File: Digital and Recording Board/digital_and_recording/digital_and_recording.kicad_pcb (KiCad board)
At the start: 4 copper layers, 47 x 106.3 mm, 40 parts, among them J1 Headphones, J2 Screen, J3 USB_Breakout, J4 Joystick, J6 MINIFIT-2-VERT, J7 MINIFIT-2-VERT, J8 MINIFIT-2-VERT, U1 Daisy_Seed, U2 Daisy_Seed_Recording, U3 Bypass 2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

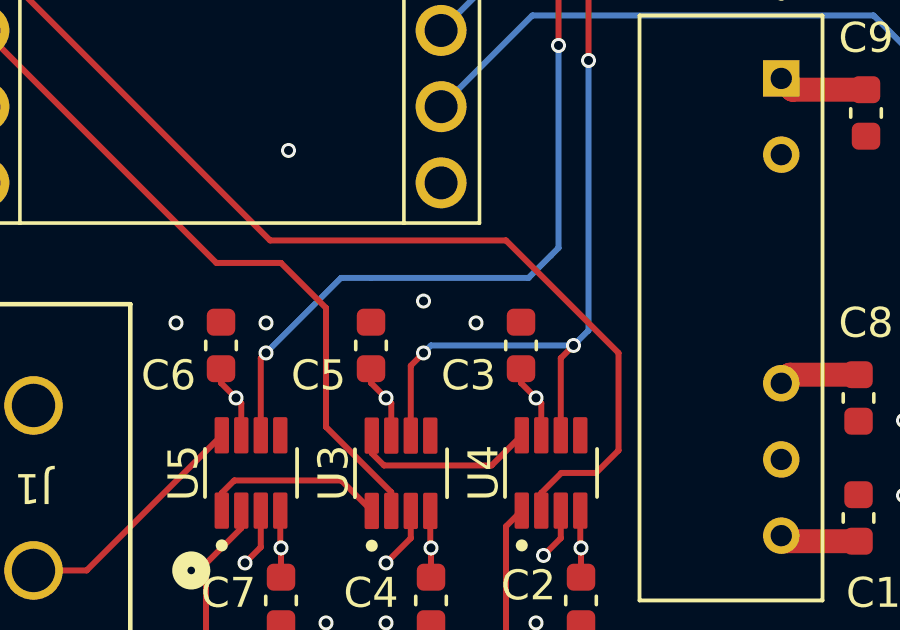
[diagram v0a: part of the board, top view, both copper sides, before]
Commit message: Reduced minimum clearance on digicorder
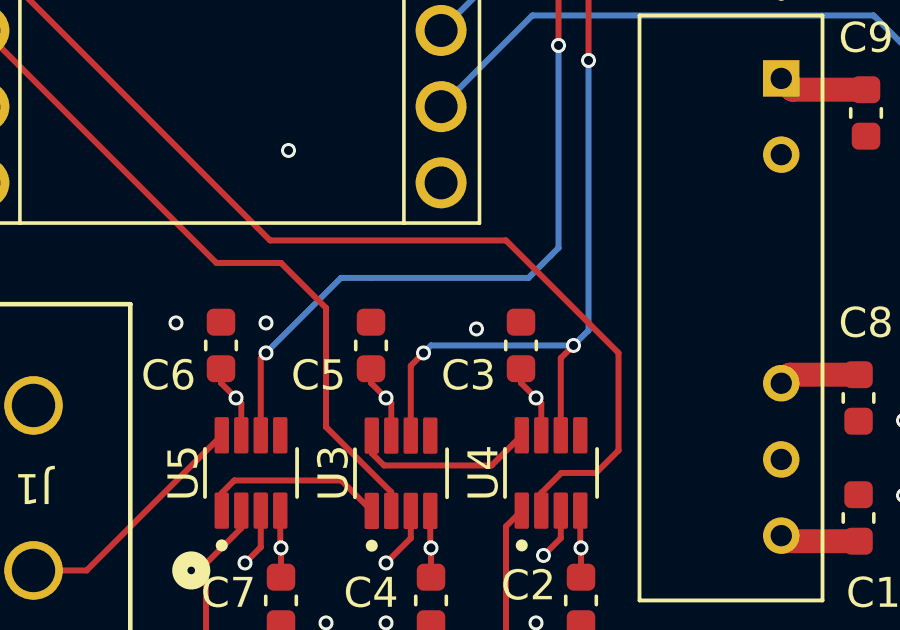
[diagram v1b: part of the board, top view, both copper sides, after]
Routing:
- net GND: vias 51 -> 50
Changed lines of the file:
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@@
 	)
 	(via
-		(at 147 128.75)
+		(at 147.0152 128.95)
 		(size 0.5)
 		(drill 0.3)
@@
 	(via
 		(at 134.25 117.25)
-		(size 0.5)
-		(drill 0.3)
-		(layers "F.Cu" "B.Cu")
-		(free yes)
-		(net 1)
-	)
-	(via
-		(at 145.25 128.02)
 		(size 0.5)
 		(drill 0.3)
@@
 		(priority 5)
 		(connect_pads
-			(clearance 0.5)
+			(clearance 0.25)
 		)
 		(min_thickness 0.25)
@@
 		(priority 3)
 		(connect_pads
-			(clearance 0.5)
+			(clearance 0.25)
 		)
 		(min_thickness 0.25)
@@
 		(polygon
 			(pts
-				(xy 157.7 154.4) (xy 157.7 139.8) (xy 158.5 139) (xy 158.5 139) (xy 160.25 137.249999) (xy 160.25 129.5)
-				(xy 159.25 128.5) (xy 127.5 128.5) (xy 127.5 48.25) (xy 134.23 48.25) (xy 134.23 76.309999) (xy 144.726 88.555333)
+				(xy 157.7 154.4) (xy 157.7 139.8) (xy 158.5 139) (xy 160.25 137.249999) (xy 160.25 129.5) (xy 159.25 128.5)
+				(xy 127.5 128.5) (xy 127.5 48.25) (xy 134.23 48.25) (xy 134.23 76.309999) (xy 144.726 88.555333)
 				(xy 144.726 111.726) (xy 150 117) (xy 158.75 117) (xy 166.3 124.55) (xy 166.3 130.825) (xy 167.725 132.25)
 				(xy 174.5 132.25) (xy 174.5 154.4)

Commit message: changes for digital and recording board. pass to marco
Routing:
- net GND: vias 50 -> 51
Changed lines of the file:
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@@
 	)
 	(via
-		(at 173 133.5)
+		(at 173 135)
 		(size 0.5)
 		(drill 0.3)
@@
 	)
 	(via
-		(at 173 131.25)
+		(at 173 129)
 		(size 0.5)
 		(drill 0.3)
@@
 	(via
 		(at 142.25 89.75)
+		(size 0.5)
+		(drill 0.3)
+		(layers "F.Cu" "B.Cu")
+		(free yes)
+		(net 1)
+	)
+	(via
+		(at 148 87)
 		(size 0.5)
 		(drill 0.3)
@@
 	)
 	(via
-		(at 173 132)
+		(at 173 131)
 		(size 0.5)
 		(drill 0.3)

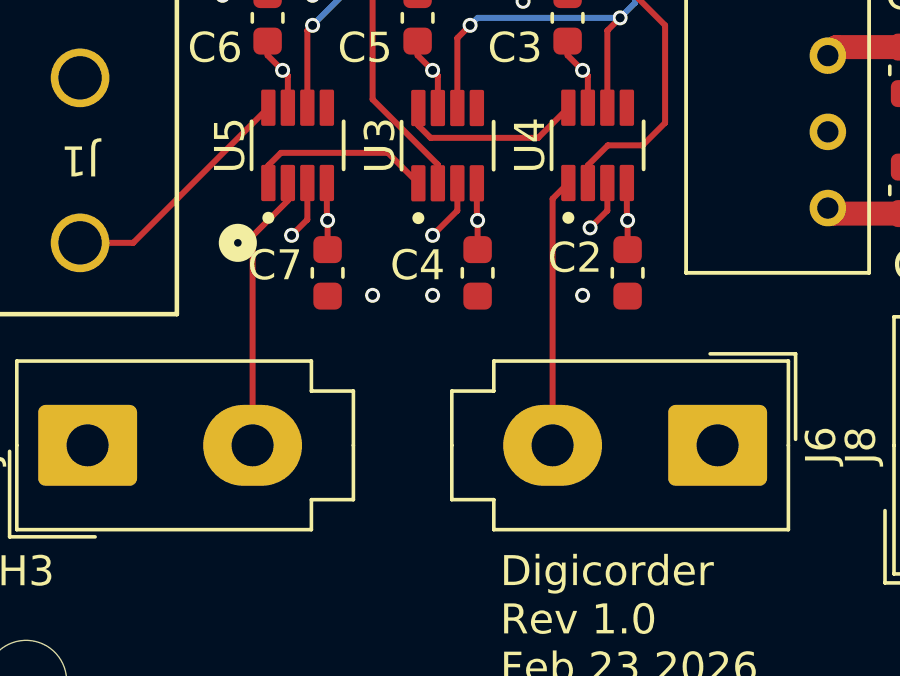
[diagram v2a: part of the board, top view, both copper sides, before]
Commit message: added buffers and caps for op-amps on effect boards
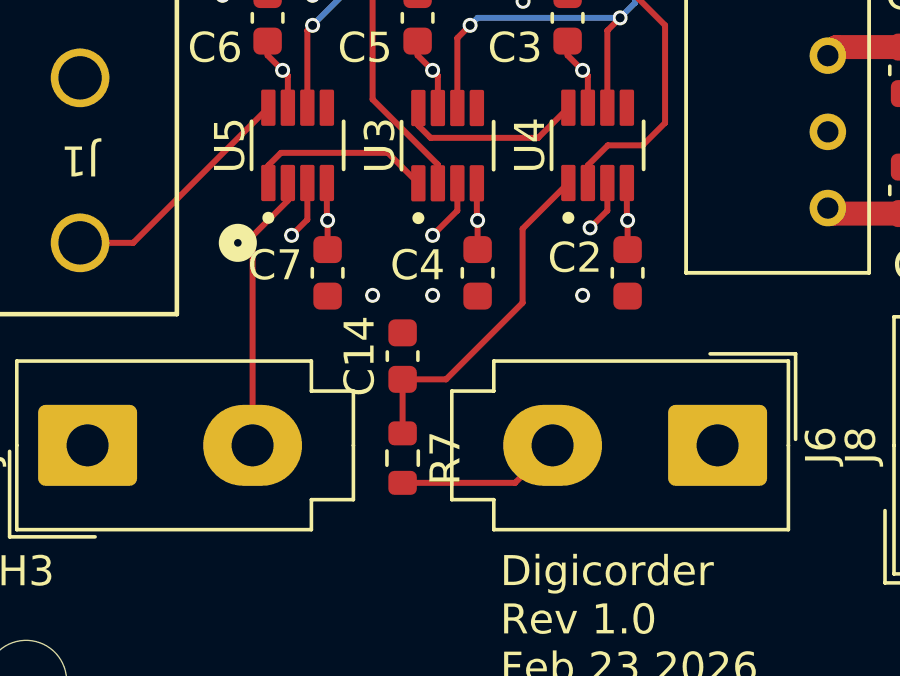
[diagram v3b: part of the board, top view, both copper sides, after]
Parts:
- added C14: 0.1u, Capacitor_SMD:C_0603_1608Metric, F.Cu at (143.0, 140.8)
- added R7: 240, Resistor_SMD:R_0603_1608Metric, F.Cu at (143.0, 144.2)
- J1: footprint Kyle's Footprints:CONN_SD-5566-002_02_MOL -> footprints:CONN_SD-5566-002_02_MOL
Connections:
- J6 pad 2: /Connectors/Guitar_In -> Net-(J6-Pad2)
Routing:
- net Net-(J6-Pad2): track 0.00 -> 5.12 mm
- net /Connectors/Guitar_In: track 8.96 -> 11.5 mm
